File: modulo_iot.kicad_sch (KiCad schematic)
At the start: 55 parts, among them J1 SMA_CONNECTOR, Q10 BC817, Q2 BC817, Q3 BC817, Q4 BC817, Q5 BC817, Q6 BC817, Q7 BC817, Q8 BC817, Q9 BC817, U6 BG95-M3

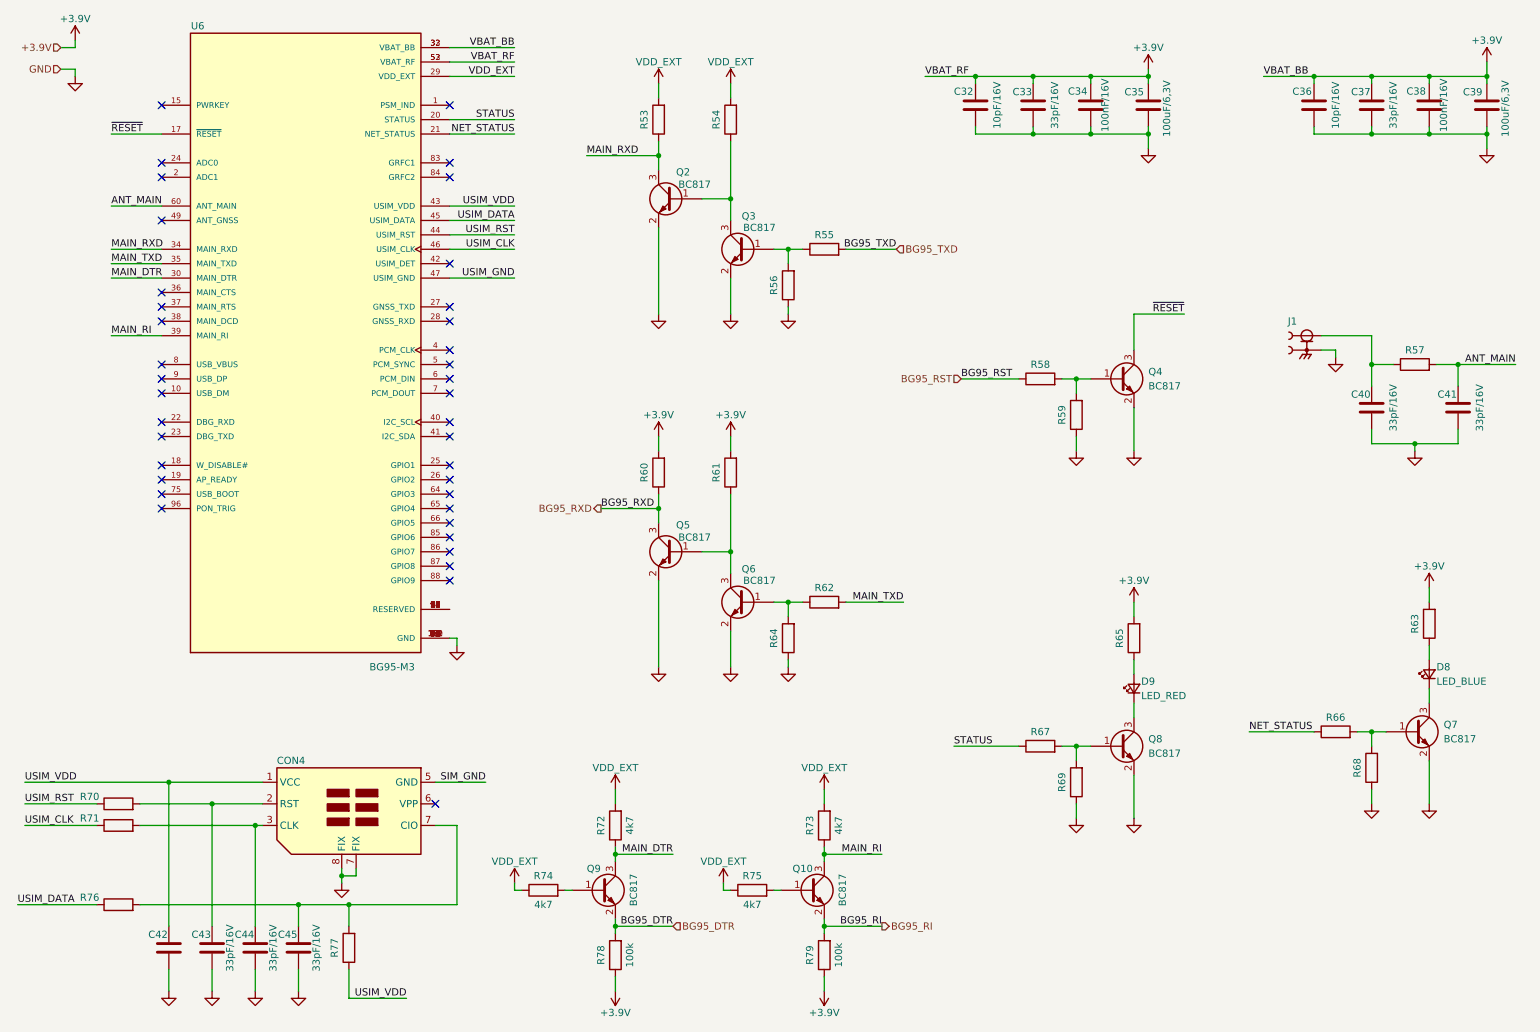
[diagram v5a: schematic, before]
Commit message: Corrigido todos os ERC
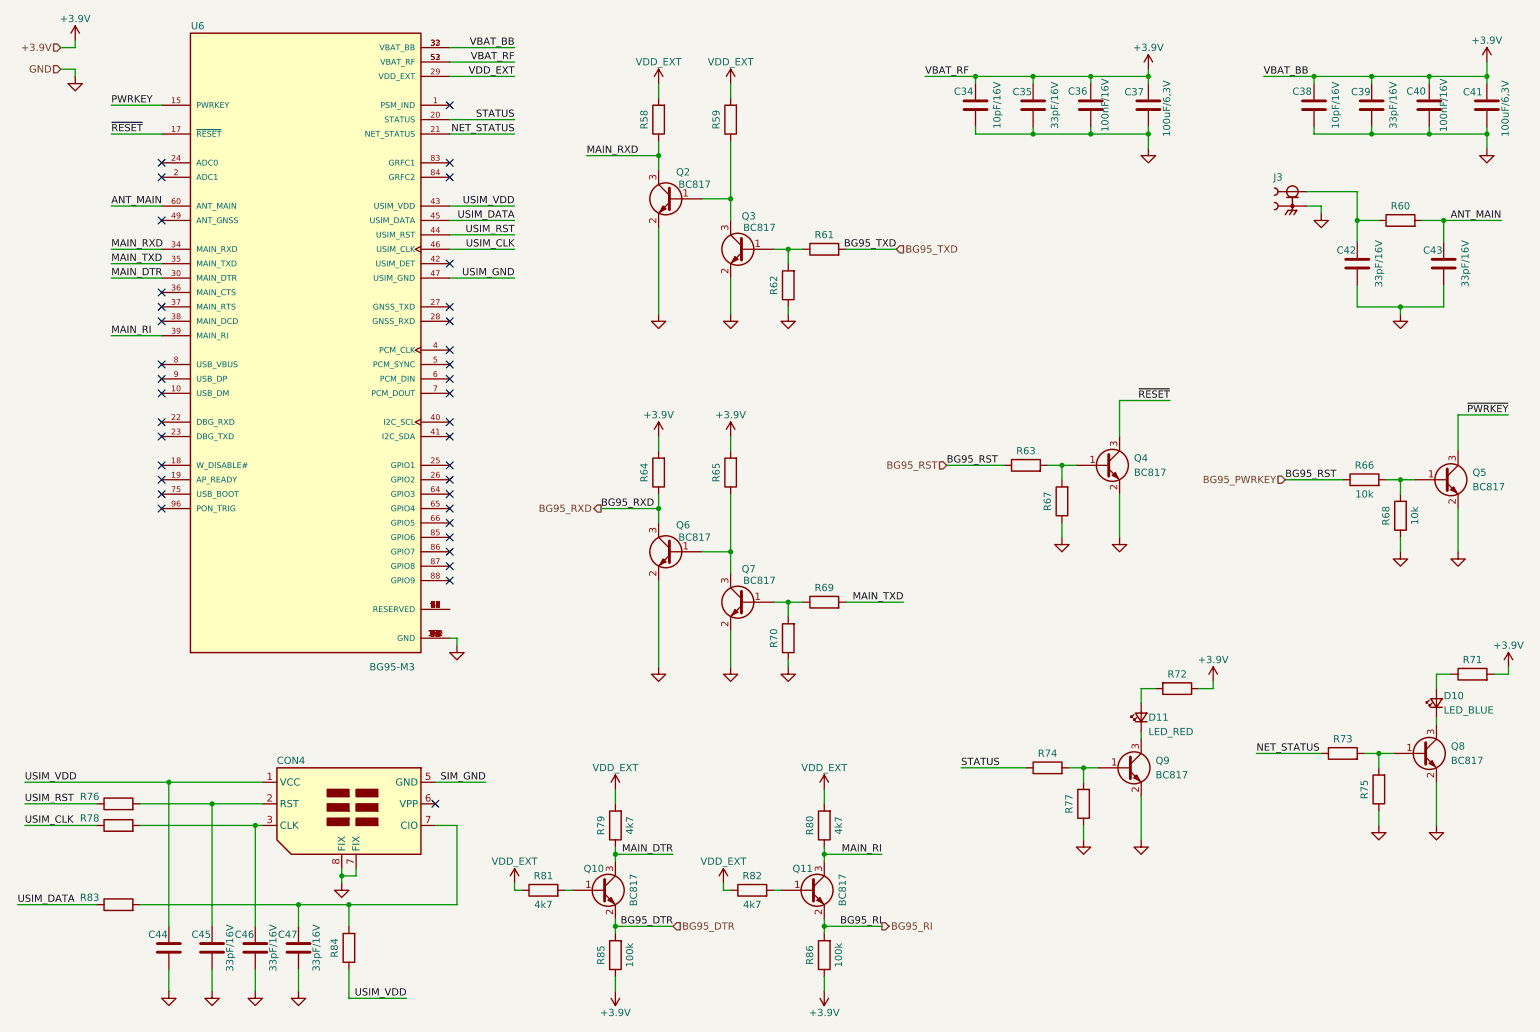
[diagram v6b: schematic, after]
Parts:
- added Q5: BC817, Package_TO_SOT_SMD:SOT-23, symbol Transistor_BJT:BC817
- added R66, R68: 10k, Resistor_SMD:R_0603_1608Metric_Pad0.98x0.95mm_HandSolder, symbol Device:R
- renumbered C32 to C34, C33 to C35, C34 to C36, C35 to C37, C36 to C38, C37 to C39, C38 to C40, C39 to C41, C40 to C42, C41 to C43, C42 to C44, C43 to C45, C44 to C46, C45 to C47, D8 to D10, D9 to D11, J1 to J3, Q9 to Q10, Q10 to Q11, Q5 to Q6, Q6 to Q7, Q7 to Q8, Q8 to Q9, R53 to R58, R54 to R59, R57 to R60, R55 to R61, R56 to R62, R58 to R63, R60 to R64, R61 to R65, R59 to R67, R62 to R69, R64 to R70, R63 to R71, R65 to R72, R66 to R73, R67 to R74, R68 to R75, R70 to R76, R69 to R77, R71 to R78, R72 to R79, R73 to R80, R74 to R81, R75 to R82, R76 to R83, R77 to R84, R78 to R85, R79 to R86
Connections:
- net GND: now also Q5.2 (E), R68.1
- net at R72.1: no longer D11.2 (A)
- net at R72.2: now also D11.2 (A)
- net PWRKEY: now reaches U6.15 (PWRKEY)
- net BG95_RST renamed BG95_PWRKEY
- net BG95_PWRKEY: now also R66.1
- new net: Q5.1 (B), R66.2, R68.2
- new net ~{PWRKEY}: Q5.3 (C)
- no-connect marks 38 -> 37
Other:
- moved on the sheet: C42, C43, D10, D11, J3, Q4, Q8, Q9, R60, R63, R67, R71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

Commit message: Corrigido a net do ~{PWRKEY}
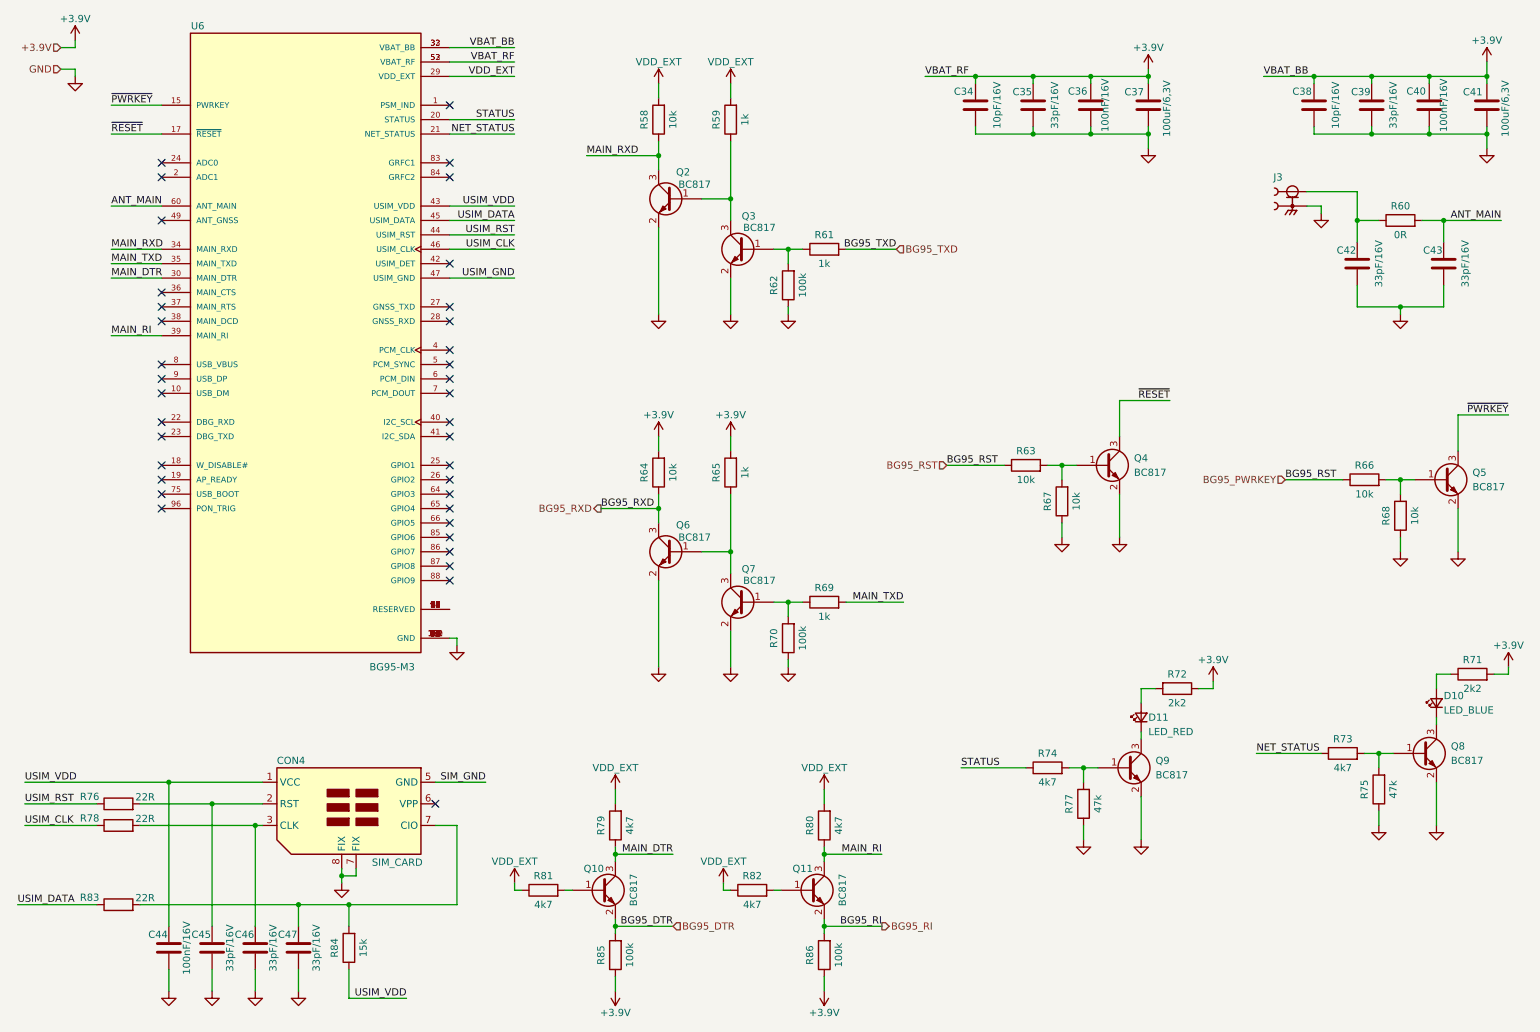
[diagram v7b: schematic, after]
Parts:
- C44: value (none) -> 100nF/16V; footprint (none) -> Capacitor_SMD:C_0402_1005Metric_Pad0.74x0.62mm_HandSolder
- CON4: value (none) -> SIM_CARD; footprint (none) -> Alexandre_Library:SIM_CARD_SIMPLES
- R58, R63, R64, R67: value (none) -> 10k; footprint (none) -> Resistor_SMD:R_0603_1608Metric_Pad0.98x0.95mm_HandSolder
- R59, R61, R65, R69: value (none) -> 1k; footprint (none) -> Resistor_SMD:R_0603_1608Metric_Pad0.98x0.95mm_HandSolder
- R60: value (none) -> 0R; footprint (none) -> Resistor_SMD:R_0603_1608Metric_Pad0.98x0.95mm_HandSolder
- R62, R70: value (none) -> 100k; footprint (none) -> Resistor_SMD:R_0603_1608Metric_Pad0.98x0.95mm_HandSolder
- R71, R72: value (none) -> 2k2; footprint (none) -> Resistor_SMD:R_0603_1608Metric_Pad0.98x0.95mm_HandSolder
- R73, R74: value (none) -> 4k7; footprint (none) -> Resistor_SMD:R_0603_1608Metric_Pad0.98x0.95mm_HandSolder
- R75, R77: value (none) -> 47k; footprint (none) -> Resistor_SMD:R_0603_1608Metric_Pad0.98x0.95mm_HandSolder
- R76, R78, R83: value (none) -> 22R; footprint (none) -> Resistor_SMD:R_0603_1608Metric_Pad0.98x0.95mm_HandSolder
- R84: value (none) -> 15k; footprint (none) -> Resistor_SMD:R_0603_1608Metric_Pad0.98x0.95mm_HandSolder
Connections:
- net PWRKEY is gone; now on net ~{PWRKEY}: U6.15 (PWRKEY)

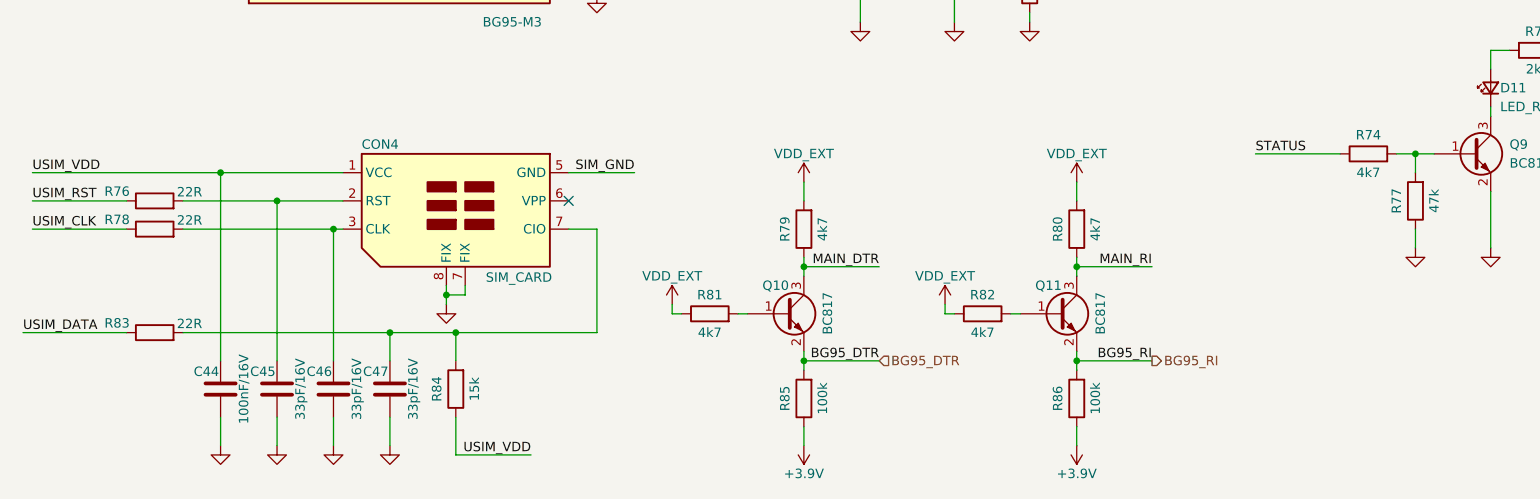
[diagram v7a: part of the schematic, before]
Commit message: Criado um sheet para o SIM Card
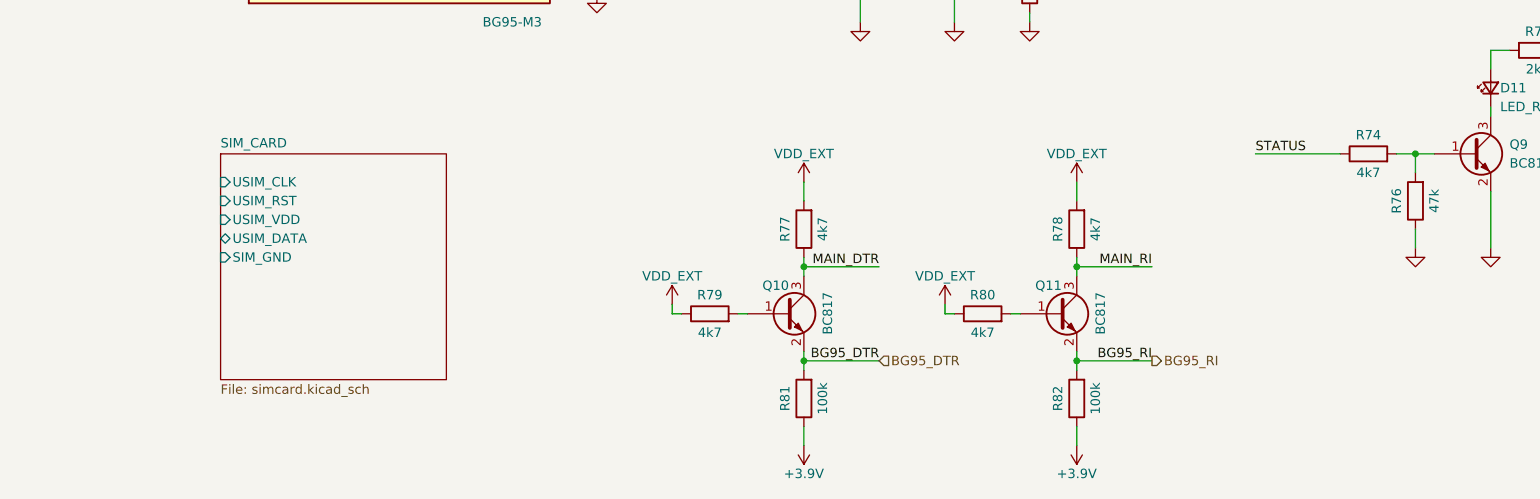
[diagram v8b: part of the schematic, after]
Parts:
- removed C44: 100nF/16V, Capacitor_SMD:C_0402_1005Metric_Pad0.74x0.62mm_HandSolder, symbol Device:C
- removed C45, C46, C47: 33pF/16V, Capacitor_SMD:C_0402_1005Metric_Pad0.74x0.62mm_HandSolder, symbol Device:C
- removed CON4: SIM_CARD, Alexandre_Library:SIM_CARD_SIMPLES, symbol Alexandre_Library:SIM_CARD
- removed R76, R78, R83: 22R, Resistor_SMD:R_0603_1608Metric_Pad0.98x0.95mm_HandSolder, symbol Device:R
- removed R84: 15k, Resistor_SMD:R_0603_1608Metric_Pad0.98x0.95mm_HandSolder, symbol Device:R
- renumbered R77 to R76, R79 to R77, R80 to R78, R81 to R79, R82 to R80, R85 to R81, R86 to R82
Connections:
- no-connect marks 37 -> 36
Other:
- added sheet SIM_CARD (simcard.kicad_sch)
